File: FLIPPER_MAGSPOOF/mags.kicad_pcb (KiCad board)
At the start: 2 copper layers, 66 x 30.5 mm, 29 parts, among them J1 Coil, J2 Conn_01x10_Socket, J3 Conn_01x08_Socket, J4 Conn_01x08_Socket, J5 Conn_01x10_Socket, SW1 On, U1 TC4424

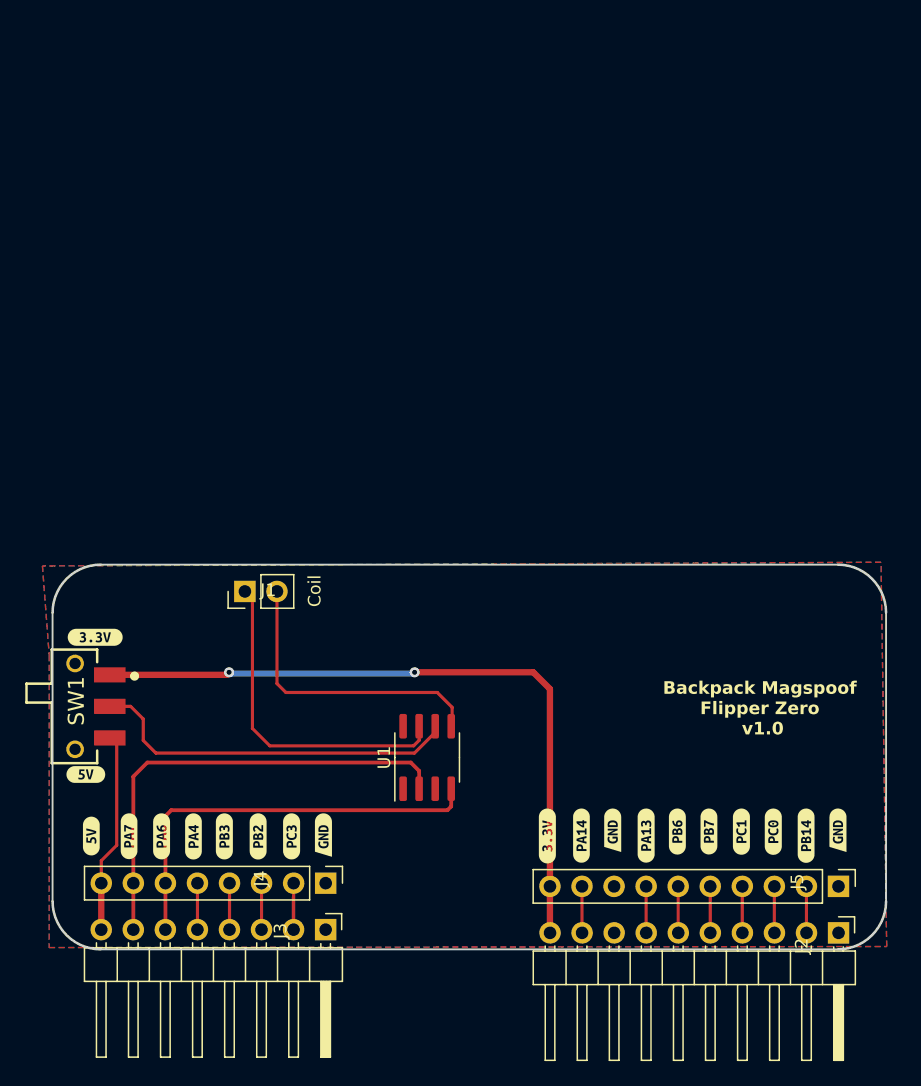
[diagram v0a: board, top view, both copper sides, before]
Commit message: feat(Hw): Coil changed
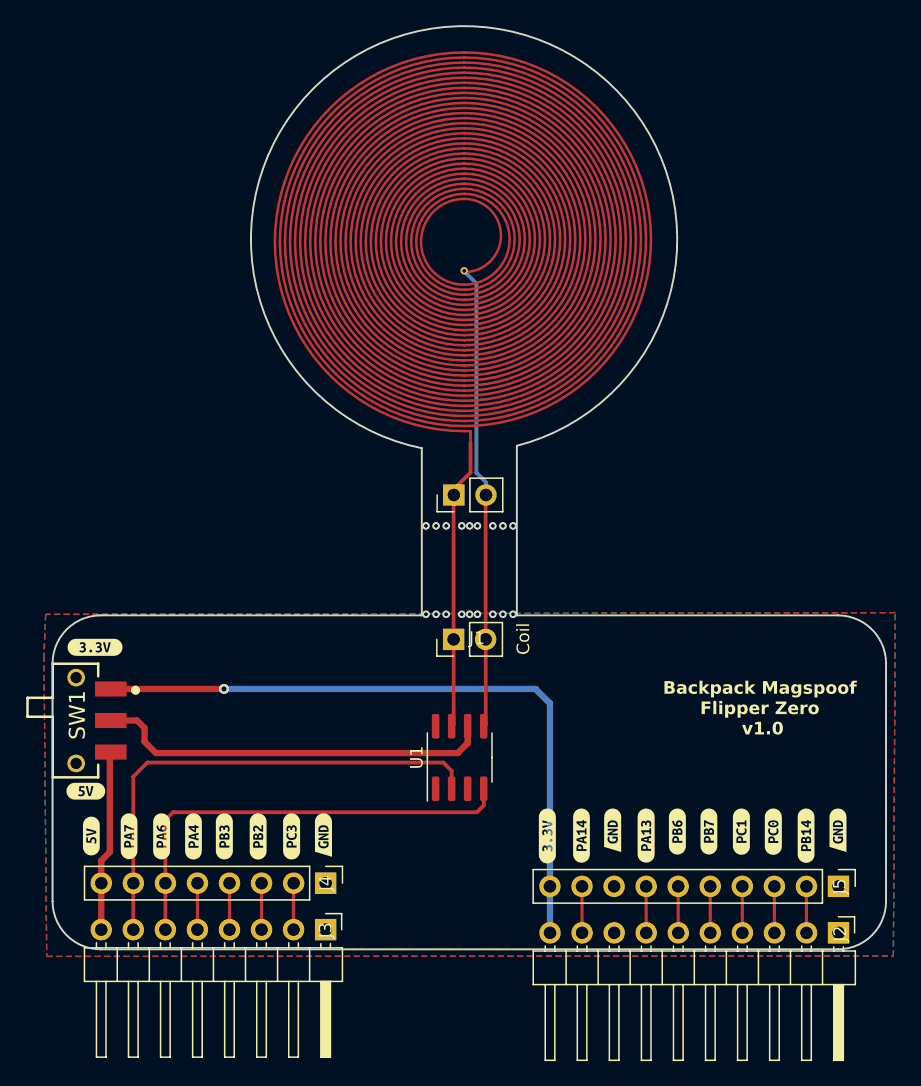
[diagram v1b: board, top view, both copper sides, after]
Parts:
- added J6: Coil, Connector_PinHeader_2.54mm:PinHeader_1x02_P2.54mm_Vertical, F.Cu at (228.0, 50.6)
- added L1: 30t_30mm, Library:Coil_30t_30mm_0.2_0.2_0.6_0.3, F.Cu at (228.8, 30.4)
- moved J1 17.0 mm to (228.0, 62.1)
- moved U1 2.57 mm to (228.5, 71.5)
- moved kibuzzard-649DB344 1.32 mm to (198.8, 74.1)
- moved SW1 1.12 mm to (199.8, 68.5)
- moved kibuzzard-6488F75A 0.79 mm to (199.6, 62.7)
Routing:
- net /Out_B: track 23.5 -> 36.9 mm
- net /Out_A: track 26.2 -> 23.1 mm
- net /IN_A: track 36.9 -> 39.5 mm
- net /IN_B: track 33.4 -> 35.7 mm
- net /VDD: track 29.5 -> 31.6 mm
- net +5V: track 15.9 -> 14.4 mm
- net +3V3: track 54.9 -> 53.5 mm, vias 2 -> 1
- net GND: vias 0 -> 9
- net (no net): vias 0 -> 9
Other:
- board size 66 x 30.5 mm -> 66 x 73.1 mm
- board text added: "${REFERENCE}"

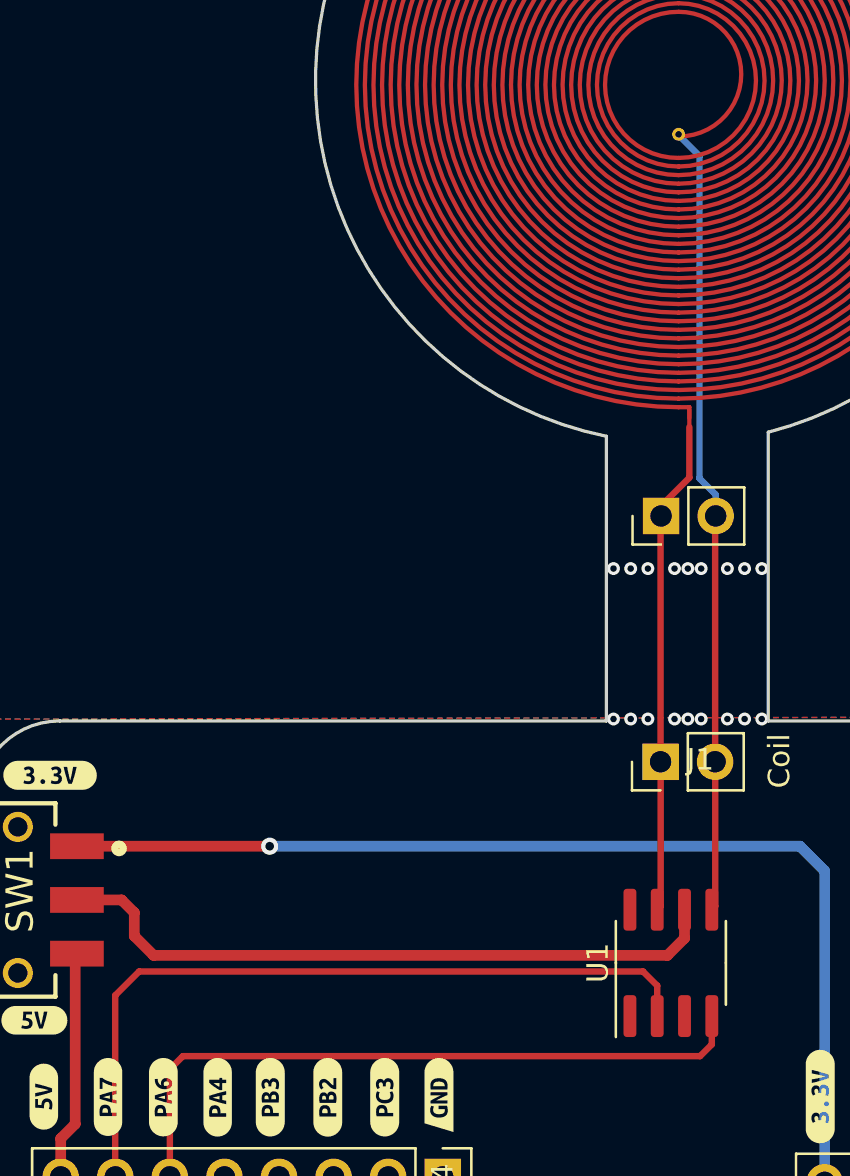
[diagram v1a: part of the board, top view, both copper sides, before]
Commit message: feat(Hw): add capacitor formosfet driver
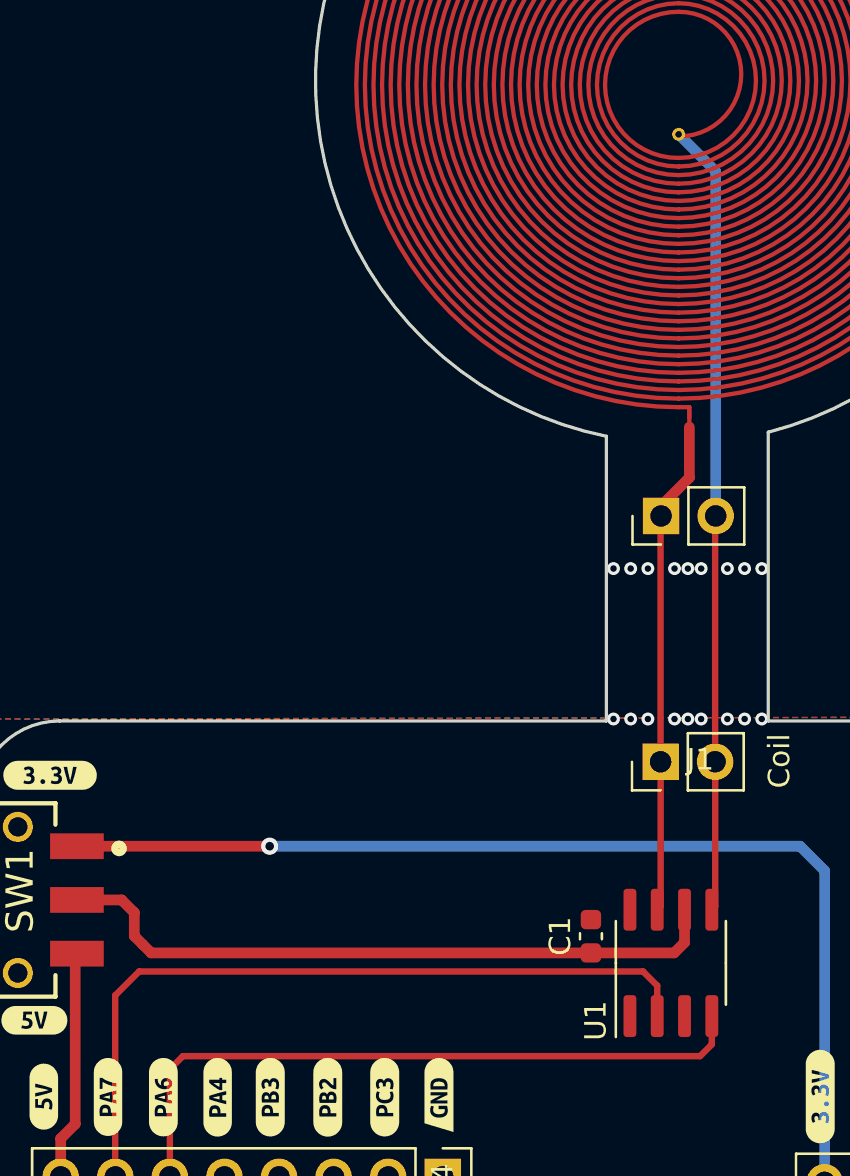
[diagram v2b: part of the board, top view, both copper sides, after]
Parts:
- removed G***: LOGO, Aesthetics:electronic_cats_logo_4x3
- removed REF**: OSHW-Logo_11.4x12mm_SilkScreen, Symbol:OSHW-Logo_11.4x12mm_SilkScreen
- added C1: 10uF, Capacitor_SMD:C_0603_1608Metric, F.Cu at (224.8, 70.2)

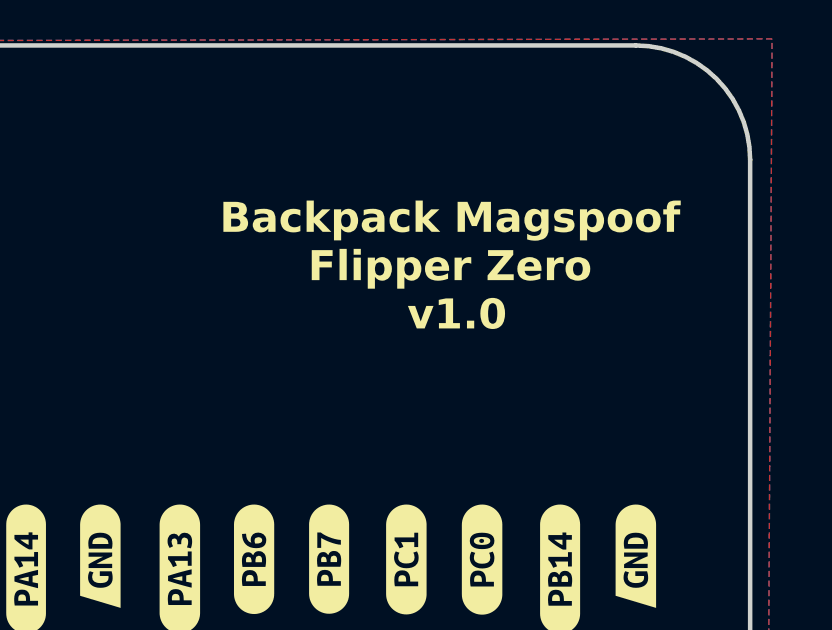
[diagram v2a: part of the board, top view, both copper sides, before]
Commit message: fix (hw): update version label and change dimensions layer
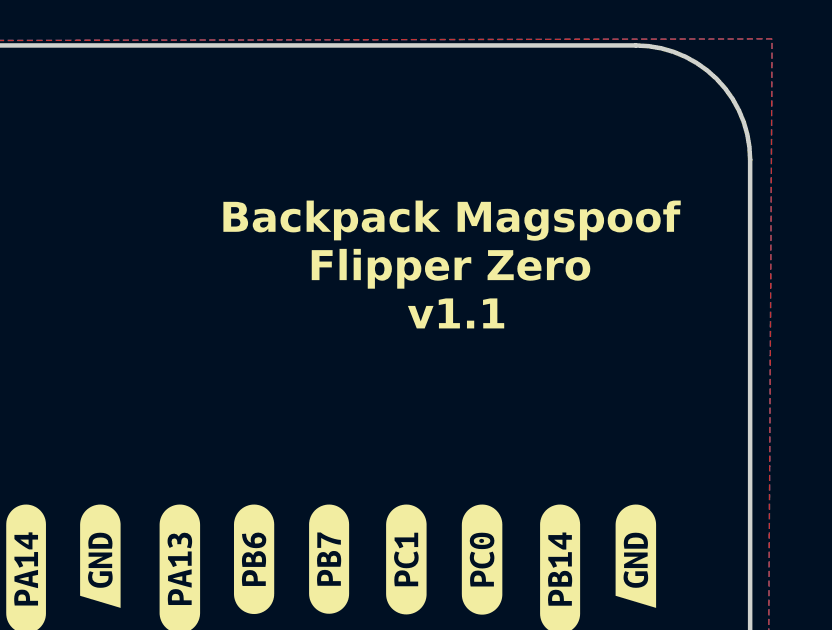
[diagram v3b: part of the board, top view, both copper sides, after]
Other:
- board text added: "Backpack Magspoof Flipper Zero v1.1"
- board text removed: "Backpack Magspoof Flipper Zero v1.0"

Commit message: fix(fw): add thickness comment
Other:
- board text added: "PCB tickness = 0.8 mm"
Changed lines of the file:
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@@
+		)
+	)
+	(gr_text "PCB tickness = 0.8 mm"
+		(at 197.25 105.86 0)
+		(layer "Cmts.User")
+		(effects
+			(font
+				(size 1 1)
+				(thickness 0.15)
+			)
+			(justify left bottom)
 		)
 	)

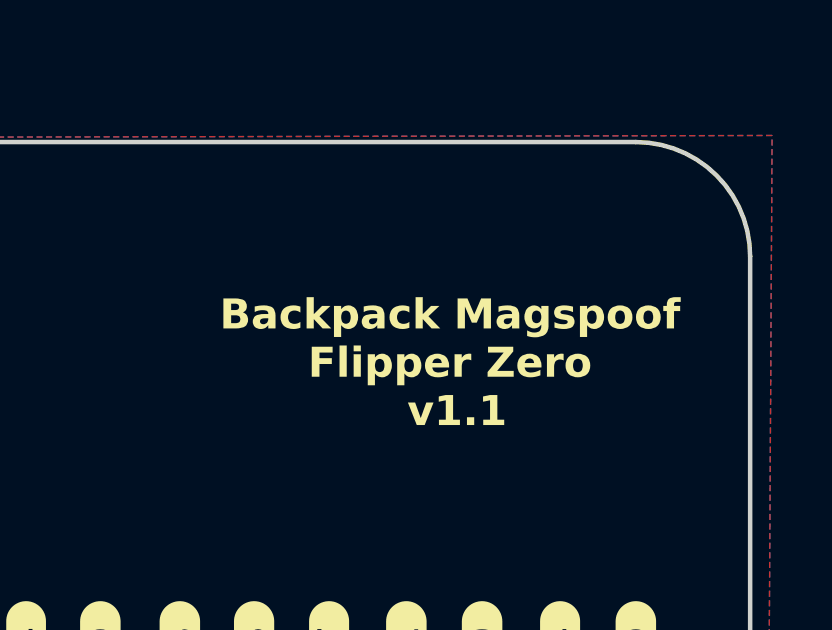
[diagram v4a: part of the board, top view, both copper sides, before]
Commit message: feat: rename addons
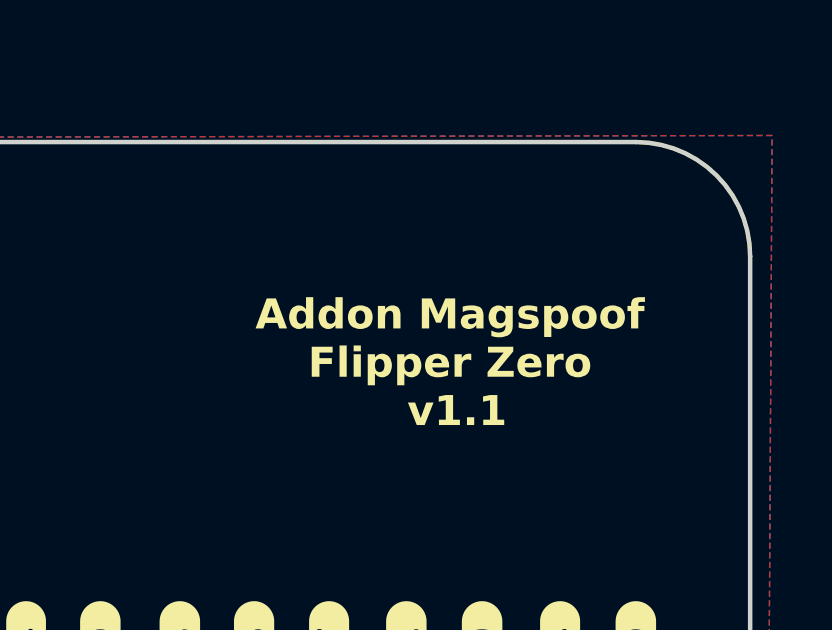
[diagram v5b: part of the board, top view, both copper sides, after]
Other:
- board text added: "Addon Magspoof Flipper Zero v1.1"
- board text removed: "Backpack Magspoof Flipper Zero v1.1"
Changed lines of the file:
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@@
 		(layer "Edge.Cuts")
 	)
-	(gr_text "Backpack Magspoof\nFlipper Zero\n v1.1"
+	(gr_text "Addon Magspoof\nFlipper Zero\n v1.1"
 		(at 254.2 72.75 0)
 		(layer "B.SilkS")
@@
 		)
 	)
-	(gr_text "Backpack Magspoof\nFlipper Zero\n v1.1"
+	(gr_text "Addon Magspoof\nFlipper Zero\n v1.1"
 		(at 252.25 67.55 0)
 		(layer "F.SilkS")

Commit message: feat(hw): change SW1 part and footprint
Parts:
- SW1: footprint footprintsg:JS102011SAQN -> Library:MSK12C02
- moved SW1 1.87 mm to (198.0, 68.3)
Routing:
- net +3V3: track 53.5 -> 54.4 mm
- net /VDD: track 31.7 -> 32.2 mm
